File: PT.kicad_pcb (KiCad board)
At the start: 4 copper layers, 67 x 68 mm, 106 parts, among them J1 Conn_02x05_Odd_Even, J10 Screw_Terminal_01x05, J11 RJ45_Hanrun_HR911105A_Horizon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, J2 USB_C_Receptacle_USB2.0_16P, J3 Conn_02x01, J4 Conn_02x01, J5 Conn_02x01, J6 Conn_02x01, J7 Screw_Terminal_01x02, J8 Conn_02x01, J9 Conn_02x01, SW1 SW_MEC_5E, U1 USBLC6-2SC6, U2 STM32H563RITx, U3 LP5907MFX-3.3, U4 ADS131A04, U5 TJA1042T-3, U6 LAN8742A, Y1 25 MHz, Y2 16.384 MHz, Y3 25 MHz

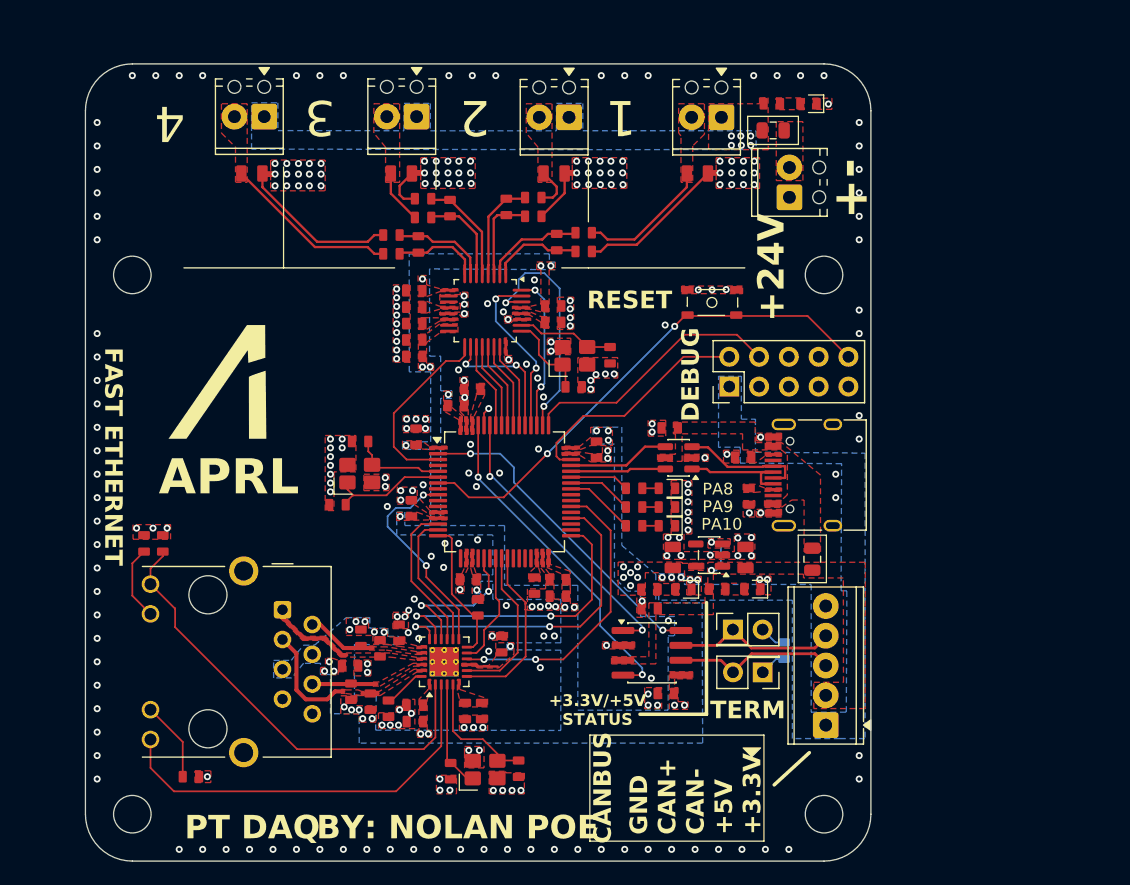
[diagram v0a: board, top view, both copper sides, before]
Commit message: Swap to STM32H563RIV6, and add split +3.3V and +3.3VA
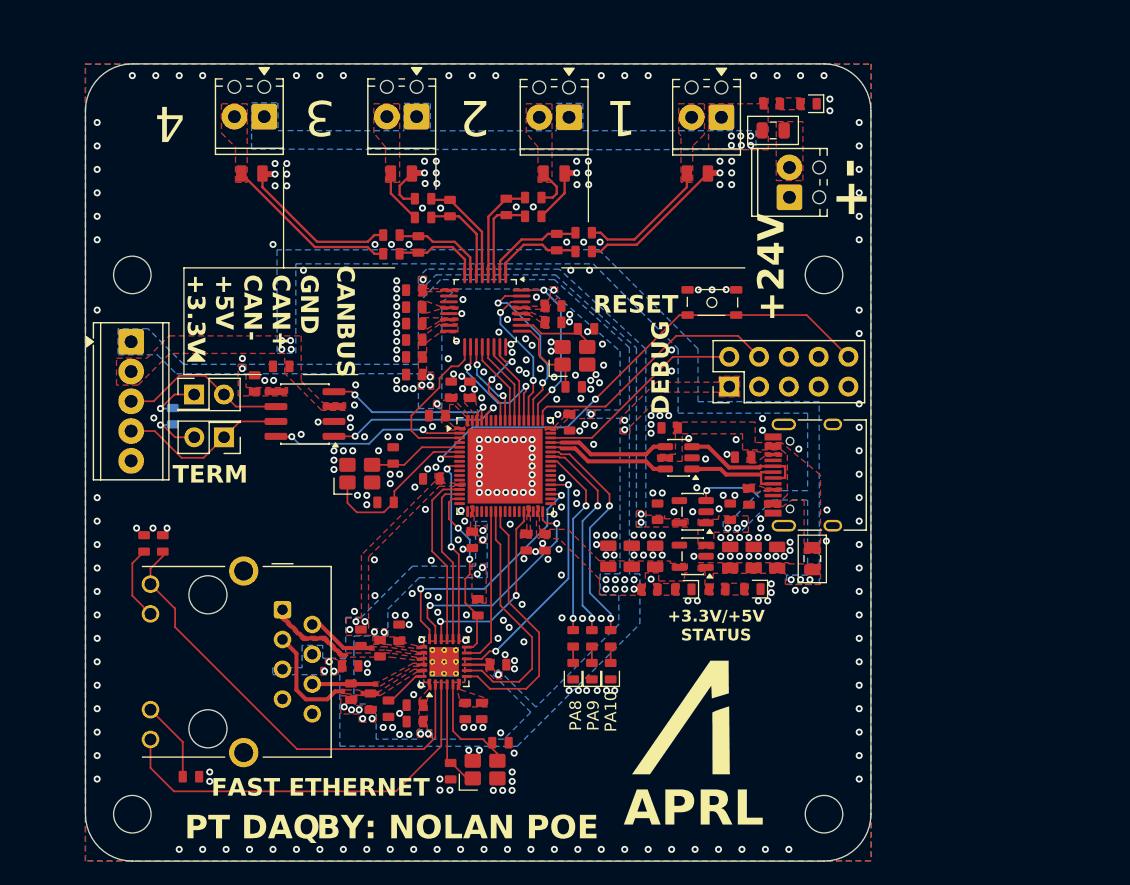
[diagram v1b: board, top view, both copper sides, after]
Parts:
- removed C1: 1uF, aprlprints:C_0603-noct
- removed C2, C3, C4, C5, C6, C7: 100nF, aprlprints:C_0603-noct
- added C39: 100nF, aprlprints:C_0603-noct, F.Cu at (128.8, 101.1)
- added C40: 100nF, aprlprints:C_0603-noct, F.Cu at (138.9, 103.9)
- added C41: 100nF, aprlprints:C_0603-noct, F.Cu at (136.8, 114.1)
- added C42: 100nF, aprlprints:C_0603-noct, F.Cu at (130.6, 113.9)
- added C43: 100nF, aprlprints:C_0603-noct, F.Cu at (127.1, 108.7)
- added C44: 100nF, aprlprints:C_0603-noct, F.Cu at (127.6, 103.3)
- added C46: 100nF, aprlprints:C_0603-noct, F.Cu at (125.7, 92.6)
- added C47: 22uF, aprlprints:C_0805-noct, F.Cu at (152.6, 115.4)
- added C48: 22uF, aprlprints:C_0805-noct, F.Cu at (154.6, 115.4)
- added C49: 22uF, aprlprints:C_0805-noct, F.Cu at (156.6, 115.4)
- added C50: 22uF, aprlprints:C_0805-noct, F.Cu at (142.2, 115.3)
- added C51: 22uF, aprlprints:C_0805-noct, F.Cu at (144.2, 115.3)
- added C52: 22uF, aprlprints:C_0805-noct, F.Cu at (146.2, 115.3)
- added U7: STM32H563RIVx, Package_DFN_QFN:QFN-68-1EP_8x8mm_P0.4mm_EP6.4x6.4mm, F.Cu at (133.4, 107.6)
- C13, C14: value 22uF -> 1uF; footprint aprlprints:C_0805-noct -> aprlprints:C_0603-noct
- SW1: value SW_MEC_5E -> SKRPANE010
- U2: value STM32H563RITx -> AP2112K-3.3; footprint Package_QFP:LQFP-64_10x10mm_P0.5mm -> Package_TO_SOT_SMD:SOT-23-5
- moved H2 74.8 mm to (101.6, 137.3)
- moved H4 74.8 mm to (160.6, 91.3)
- moved J10 67.7 mm to (101.5, 97.0), turned to -90 degrees
- moved R21 55.9 mm to (105.0, 103.4), turned to 90 degrees
- moved J9 54.0 mm to (106.9, 101.5), turned to 0 degrees
- moved REF** 48.8 mm to (150.0, 129.8)
- moved J8 46.4 mm to (109.4, 105.2), turned to 180 degrees
- moved C35 43.9 mm to (112.0, 100.6), turned to 90 degrees
- moved C32 37.6 mm to (114.3, 99.1)
- moved U5 35.9 mm to (116.3, 103.2), turned to 180 degrees
- moved U2 17.0 mm to (149.4, 115.3), turned to 180 degrees
- moved D3 16.3 mm to (142.4, 125.1), turned to 90 degrees
- moved D2 15.4 mm to (140.8, 125.1), turned to 90 degrees
- moved D1 14.8 mm to (139.2, 125.1), turned to 90 degrees
- moved R5 13.0 mm to (142.4, 122.3), turned to 90 degrees
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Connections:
- C10 pad 1: Net-(U2-PH1) -> Net-(U7-PH1)
- C14 pad 1: +3.3V -> +3.3VA
- C9 pad 1: Net-(U2-PH0) -> Net-(U7-PH0)
- U1 pad 4: USB_D+ -> /Microcontroller/USB_D+
- U1 pad 6: USB_D- -> /Microcontroller/USB_D-
- U2 pad 1: +3.3V -> +5V
- U2 pad 2: FDCAN_STDBY -> GND
- U2 pad 3: ~{ADC_RESET} -> +5V
- U2 pad 5: Net-(U2-PH0) -> +3.3V
- U3 pad 5: +3.3V -> +3.3VA
- U4 pad 9: +3.3V -> +3.3VA
- Y1 pad 1: Net-(U2-PH1) -> Net-(U7-PH1)
- Y1 pad 3: Net-(U2-PH0) -> Net-(U7-PH0)
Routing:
- net /Microcontroller/USER_LED_3: track 5.07 -> 19.5 mm, vias 0 -> 2
- net Net-(U7-PH1): track 0.00 -> 14.3 mm
- net FDCAN_RX: track 28.7 -> 14.8 mm
- net /Microcontroller/USER_LED_2: track 5.52 -> 18.0 mm, vias 0 -> 2
- net FDCAN_STDBY: track 27.7 -> 16.5 mm
- net /Microcontroller/USB_D-: track 0.00 -> 10.5 mm
- net /Microcontroller/USB_D+: track 0.00 -> 10.5 mm
- net /Microcontroller/USER_LED_1: track 5.98 -> 16.4 mm, vias 0 -> 2
- net Net-(U2-PH1): track 10.1 -> 0.00 mm
- net USB_D+: track 8.70 -> 0.00 mm
- net FDCAN_TX: track 24.6 -> 15.9 mm
- net USB_D-: track 8.12 -> 0.00 mm
- net Net-(U7-PH0): track 0.00 -> 8.08 mm
- net ETH_RXD1: track 14.8 -> 22.4 mm
- net M0: track 20.3 -> 12.7 mm
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- added copper zone on B.Cu, net +3.3VA
- added copper zone on F.Cu, net +3.3VA
- added copper zone on B.Cu, net +5V
- added copper zone on B.Cu, net GND

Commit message: June 20th is not real and cant hurt me
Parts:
- removed the REF** at (150.0, 129.8)
- added REF**: APRL_Logo_2Layer-v1, APRLPrints:APRL_Logo_2Layer-v1, F.Cu at (150.3, 129.5)
- C1: renamed from C44; footprint aprlprints:C_0603-noct -> APRLPrints:C_0603
- C10: renamed from C11; footprint aprlprints:C_0603-noct -> APRLPrints:C_0603
- C11: renamed from C12; footprint aprlprints:C_0603-noct -> APRLPrints:C_0603
- C12: renamed from C47; footprint aprlprints:C_0805-noct -> APRLPrints:C_0805
- C13: renamed from C48; footprint aprlprints:C_0805-noct -> APRLPrints:C_0805
- C14: renamed from C49; footprint aprlprints:C_0805-noct -> APRLPrints:C_0805
- C15: renamed from C50; footprint aprlprints:C_0805-noct -> APRLPrints:C_0805
- C16: renamed from C51; footprint aprlprints:C_0805-noct -> APRLPrints:C_0805
- C17: renamed from C52; footprint aprlprints:C_0805-noct -> APRLPrints:C_0805
- C18: renamed from C13; footprint aprlprints:C_0603-noct -> APRLPrints:C_0603
- C19: renamed from C14; footprint aprlprints:C_0603-noct -> APRLPrints:C_0603
- C2: renamed from C43; footprint aprlprints:C_0603-noct -> APRLPrints:C_0603
- C20: renamed from C15; footprint aprlprints:C_0603-noct -> APRLPrints:C_0603
- C21: renamed from C46; footprint aprlprints:C_0603-noct -> APRLPrints:C_0603
- C22: renamed from C16; footprint aprlprints:C_0603-noct -> APRLPrints:C_0603
- C23: renamed from C17; footprint aprlprints:C_0603-noct -> APRLPrints:C_0603
- C24: renamed from C18; footprint aprlprints:C_0603-noct -> APRLPrints:C_0603
- C25: renamed from C19; footprint aprlprints:C_0603-noct -> APRLPrints:C_0603
- C26: renamed from C20; footprint aprlprints:C_0603-noct -> APRLPrints:C_0603
- C27: renamed from C21; footprint aprlprints:C_0603-noct -> APRLPrints:C_0603
- C28: renamed from C22; footprint aprlprints:C_0603-noct -> APRLPrints:C_0603
- C29: renamed from C23; footprint aprlprints:C_0603-noct -> APRLPrints:C_0603
- C3: renamed from C42; footprint aprlprints:C_0603-noct -> APRLPrints:C_0603
- C30: renamed from C24; footprint aprlprints:C_0603-noct -> APRLPrints:C_0603
- C31: renamed from C25; footprint aprlprints:C_0603-noct -> APRLPrints:C_0603
- C32: renamed from C26; footprint aprlprints:C_0603-noct -> APRLPrints:C_0603
- C33: renamed from C27; footprint aprlprints:C_0603-noct -> APRLPrints:C_0603
- C34: renamed from C28; footprint aprlprints:C_0603-noct -> APRLPrints:C_0603
- C35: renamed from C29; footprint aprlprints:C_0603-noct -> APRLPrints:C_0603
- C36: renamed from C30; footprint aprlprints:C_0603-noct -> APRLPrints:C_0603
- C37: renamed from C31; footprint aprlprints:C_0603-noct -> APRLPrints:C_0603
- C38: renamed from C32; footprint aprlprints:C_0603-noct -> APRLPrints:C_0603
- C39: renamed from C33; footprint aprlprints:C_0603-noct -> APRLPrints:C_0603
- C4: renamed from C41; footprint aprlprints:C_0603-noct -> APRLPrints:C_0603
- C40: renamed from C34; footprint aprlprints:C_0603-noct -> APRLPrints:C_0603
- C41: renamed from C35; footprint aprlprints:C_0603-noct -> APRLPrints:C_0603
- C42: renamed from C36; footprint aprlprints:C_0603-noct -> APRLPrints:C_0603
- C43: renamed from C37; footprint aprlprints:C_0603-noct -> APRLPrints:C_0603
- C44: renamed from C38; footprint aprlprints:C_0603-noct -> APRLPrints:C_0603
- C5: renamed from C40; footprint aprlprints:C_0603-noct -> APRLPrints:C_0603
- C6: renamed from C39; footprint aprlprints:C_0603-noct -> APRLPrints:C_0603
- C7: renamed from C8; footprint aprlprints:C_0603-noct -> APRLPrints:C_0603
- C8: renamed from C9; footprint aprlprints:C_0603-noct -> APRLPrints:C_0603
- C9: renamed from C10; footprint aprlprints:C_0603-noct -> APRLPrints:C_0603
- D1: renamed from D4; footprint aprlprints:LED_0603-noct -> APRLPrints:LED_0603
- D2: renamed from D5; footprint aprlprints:LED_0603-noct -> APRLPrints:LED_0603
- D3: renamed from D6; footprint aprlprints:LED_0603-noct -> APRLPrints:LED_0603
- D4: renamed from D1; footprint aprlprints:LED_0603-noct -> APRLPrints:LED_0603
- D5: renamed from D2; footprint aprlprints:LED_0603-noct -> APRLPrints:LED_0603
- D6: renamed from D3; footprint aprlprints:LED_0603-noct -> APRLPrints:LED_0603
- F1, F2: footprint Fuse:Fuse_0805_2012Metric -> APRLPrints:Fuse_0805_2012Metric
- R1, R2, R21, R22, R23, R24, R25, R26, R27, R28, R29, R30: footprint aprlprints:R_0603-noct -> APRLPrints:R_0603
- R3: renamed from R6; footprint aprlprints:R_0603-noct -> APRLPrints:R_0603
- R4: renamed from R7; footprint aprlprints:R_0603-noct -> APRLPrints:R_0603
- R5: renamed from R8; footprint aprlprints:R_0603-noct -> APRLPrints:R_0603
- R6: renamed from R3; footprint aprlprints:R_0603-noct -> APRLPrints:R_0603
- R7: renamed from R4; footprint aprlprints:R_0603-noct -> APRLPrints:R_0603
- R8: renamed from R5; footprint aprlprints:R_0603-noct -> APRLPrints:R_0603
- SW1: footprint aprlprints:SKRPANE010-noct -> APRLPrints:SKRPANE010
- Y1, Y2, Y3: footprint aprlprints:3225-4P-L-noct -> APRLPrints:3225-4P-L
- moved U6 0.23 mm to (116.5, 103.2)
- moved C42 0.12 mm to (120.3, 124.7)
- moved C25 0.10 mm to (125.7, 99.7)
- moved R27 0.09 mm to (123.5, 128.4)
- renumbered U7 to U2, U2 to U3, U3 to U4, U4 to U5, U5 to U6, U6 to U7
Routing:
- net /Connectivity/TX+: track 7.42 -> 13.7 mm
- net /Connectivity/RX+: track 10.7 -> 16.7 mm
- net /Connectivity/RX-: track 5.47 -> 10.00 mm
- net /Connectivity/TX-: track 5.98 -> 10.3 mm
- net Net-(D1-A): track 0.00 -> 1.72 mm
- net Net-(D2-A): track 0.00 -> 1.59 mm
- net Net-(D3-A): track 0.00 -> 1.49 mm
- net /Microcontroller/USB_CONN_D-: track 8.99 -> 10.0 mm
- net Net-(C11-Pad1): track 0.63 -> 0.00 mm
- net GND: vias 386 -> 392
- removed copper zone on F.Cu, net /Connectivity/RX+
- removed copper zone on F.Cu, net /Connectivity/RX-
- removed copper zone on F.Cu, net /Connectivity/TX+
- removed copper zone on F.Cu, net /Connectivity/TX-
- removed copper zone on F.Cu, net Net-(D1-A)
- removed copper zone on F.Cu, net Net-(D2-A)
- removed copper zone on F.Cu, net Net-(D3-A)

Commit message: Timeline is not real
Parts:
- added R31: 10k, APRLPrints:R_0603, F.Cu at (136.4, 118.8)
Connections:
- U2 pad 39: ETH_RXER -> unconnected-(U2-PD12-Pad39)
- U7 pad 10: ETH_RXER -> Net-(U7-RXER/PHYAD0)
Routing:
- net ETH_RXER: track 21.0 -> 0.00 mm, vias 2 -> 0
- net Net-(U7-RXER/PHYAD0): track 0.00 -> 8.65 mm, vias 0 -> 2
- net GND: vias 392 -> 415

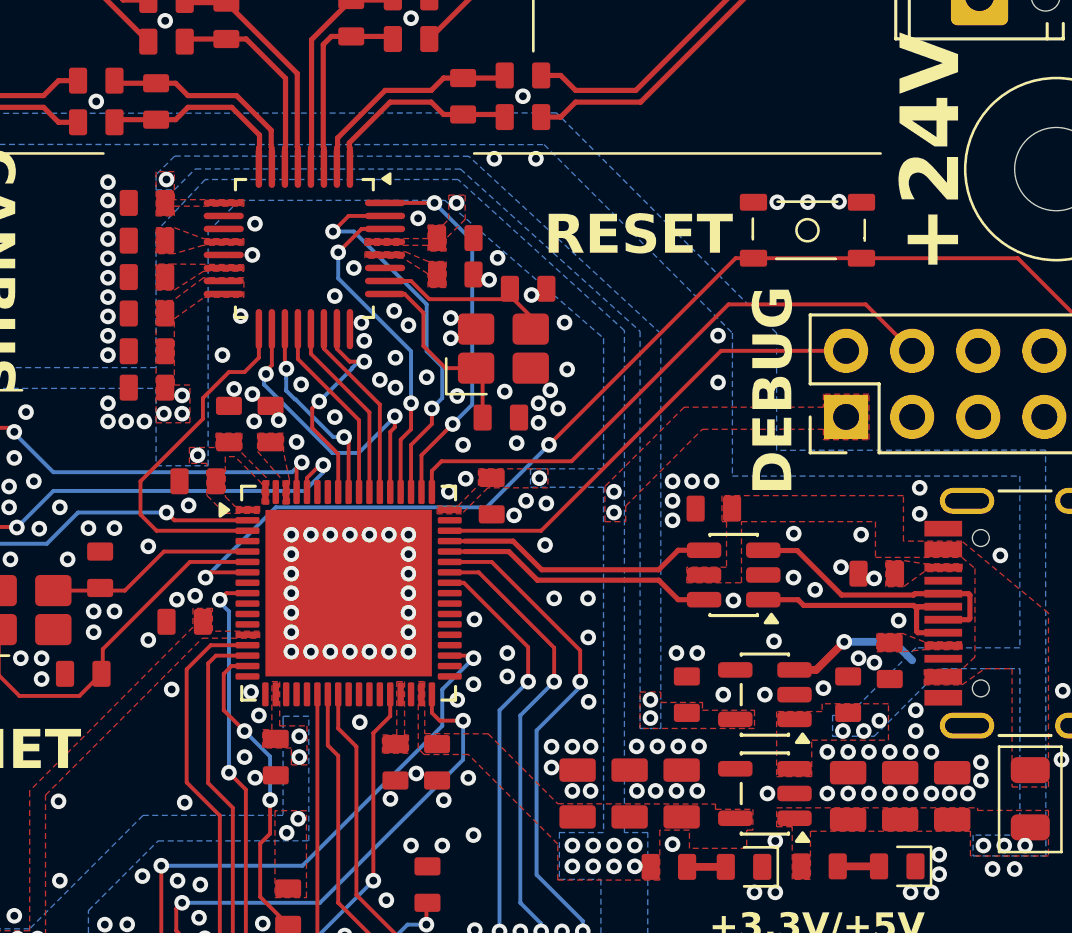
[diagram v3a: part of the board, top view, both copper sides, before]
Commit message: Remove LP5907
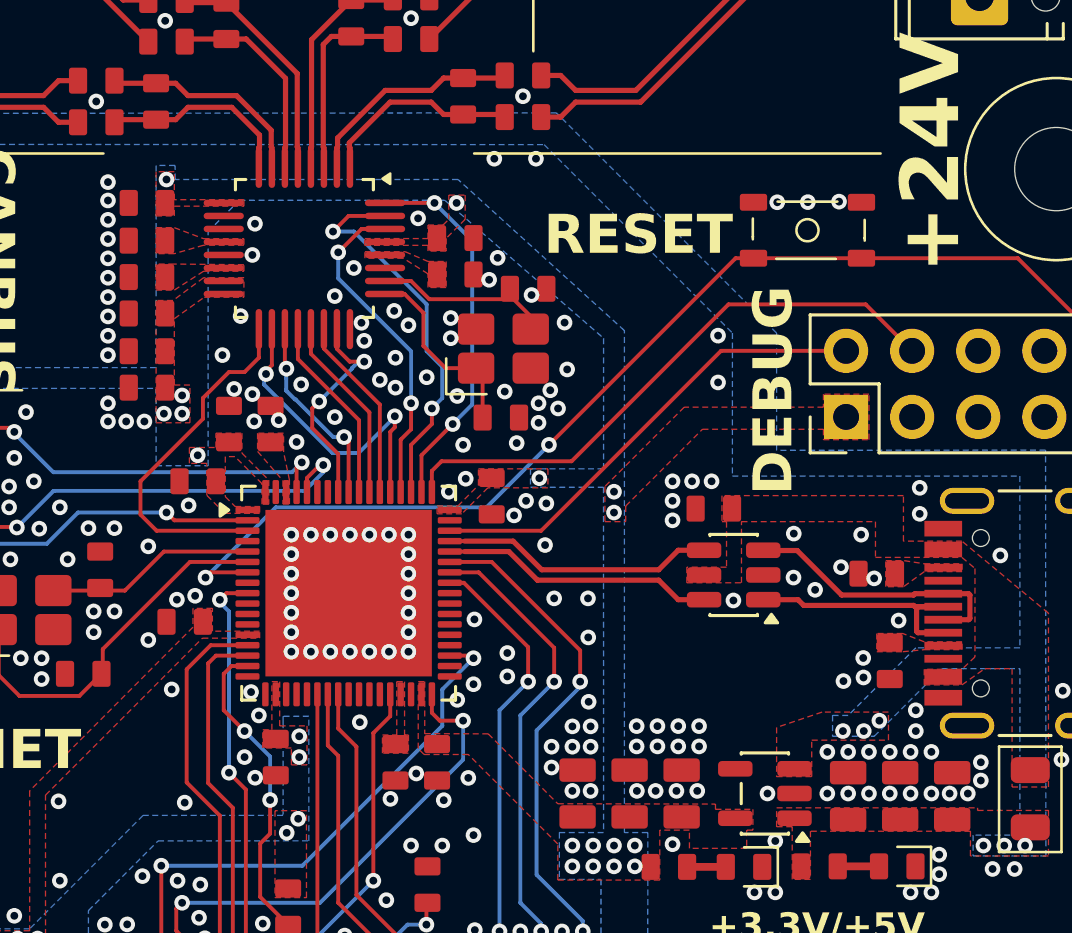
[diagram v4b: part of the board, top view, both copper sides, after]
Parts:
- removed the C18 at (152.6, 111.5)
- removed the C19 at (146.4, 111.5)
- removed the U4 at (149.4, 111.5)
- D1, D2, D3: value LED_Small -> LED
- renumbered C34 to C18, C35 to C19, C36 to C20, C37 to C21, C38 to C22, C39 to C23, C40 to C24, C41 to C25, C42 to C26, C43 to C27, C44 to C28, C20 to C29, C21 to C30, C22 to C31, C23 to C32, C24 to C33, C25 to C34, C26 to C35, C27 to C36, C28 to C37, C29 to C38, C30 to C39, C31 to C40, C32 to C41, C33 to C42, J6 to J10, J7 to J11, J8 to J3, J9 to J4, J10 to J5, J11 to J6, J3 to J7, J4 to J8, J5 to J9, R22 to R10, R23 to R11, R24 to R12, R25 to R13, R26 to R14, R31 to R15, R27 to R16, R28 to R17, R29 to R18, R30 to R19, R9 to R20, R10 to R21, R11 to R22, R12 to R23, R13 to R24, R14 to R25, R15 to R26, R16 to R27, R17 to R28, R18 to R29, R19 to R30, R20 to R31, R21 to R9, U6 to U4, U7 to U5, U5 to U6, Y3 to Y2, Y2 to Y3
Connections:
- C30 pad 1: +3.3VA -> +3.3V
- U6 pad 9: +3.3VA -> +3.3V
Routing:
- net +5V: track 5.26 -> 0.00 mm, vias 11 -> 10
- net GND: vias 415 -> 416
- net +3.3VA: vias 3 -> 0
- net +3.3V: vias 37 -> 38
- removed copper zone on B.Cu, net +3.3VA
- removed copper zone on F.Cu, net +3.3VA
